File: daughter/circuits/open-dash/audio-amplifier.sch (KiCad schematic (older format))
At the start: 28 parts, among them J12 AudioJack_3.5TRS, J13 AudioJack_3.5TRS, J14 Conn_02x03_Odd_Even, T1 Audio_Transformer, T2 Audio_Transformer, T3 Audio_Transformer, T4 Audio_Transformer, U7 TDA7851F

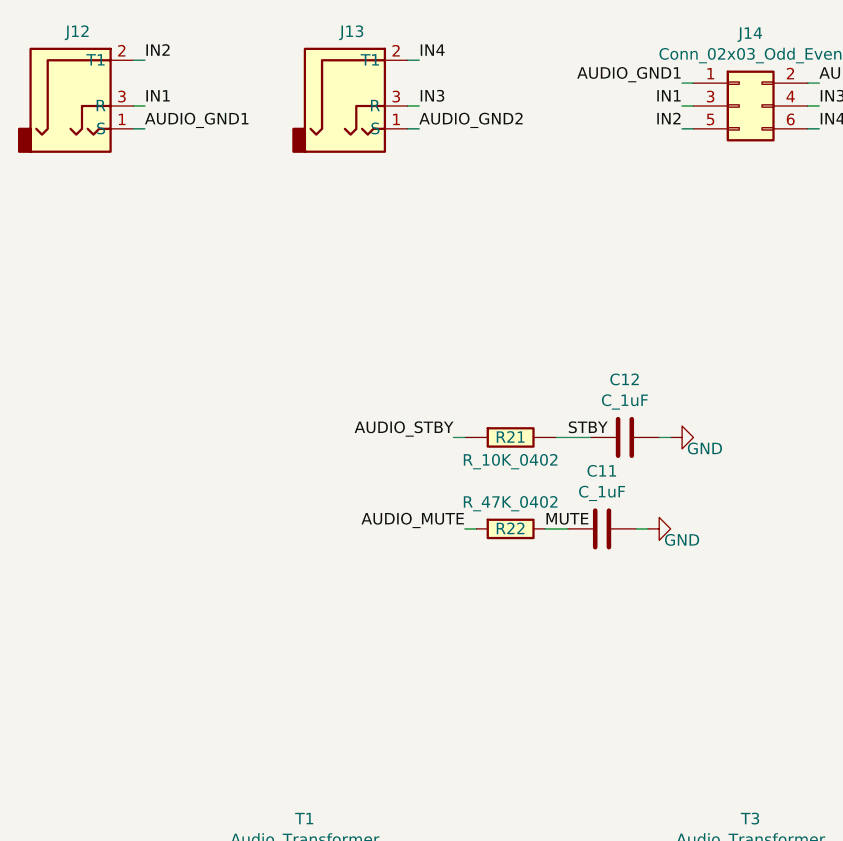
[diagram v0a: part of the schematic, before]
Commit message: send v1.4 to board house. Corrected source-drain on fets.
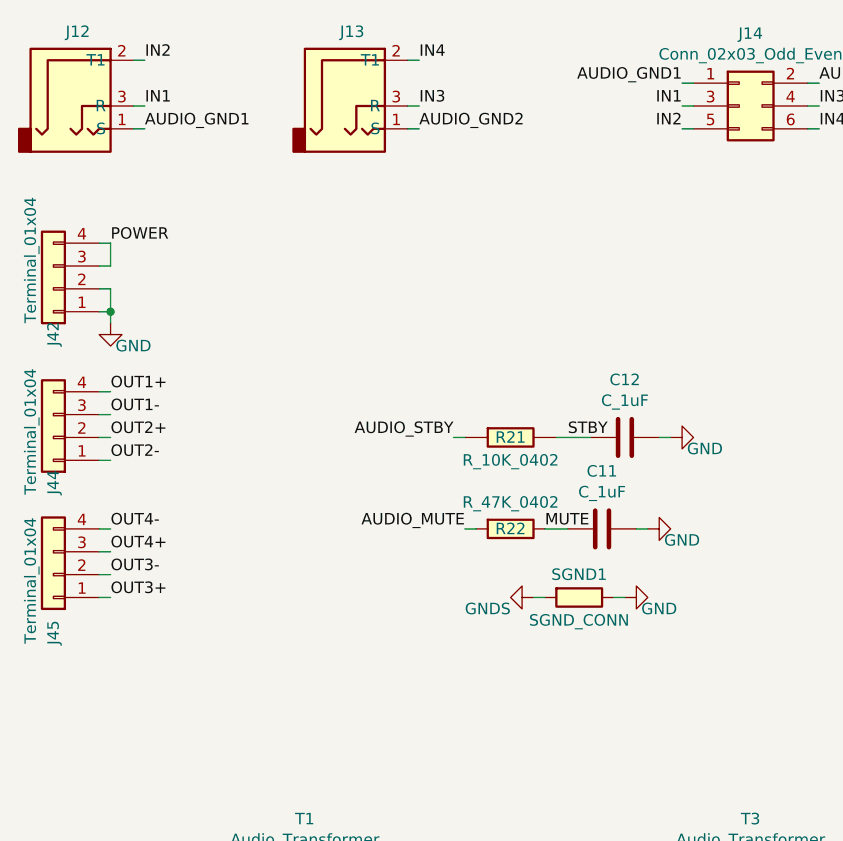
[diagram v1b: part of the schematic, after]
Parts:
- added J42, J44, J45: Terminal_01x04, Open_Automation:Terminal_1,5_4-G-5.08_1x04_P5.08mm_Horizontal, symbol Open_Automation:Terminal_01x04
- added SGND1: SGND_CONN, Open_Automation:SGND_CONN, symbol Open_Automation:SGND_CONN
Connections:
- net AUDIO_POWER: now also J42.3 (Pin_3), J42.4 (Pin_4)
- net GND: now also J42.1 (Pin_1), J42.2 (Pin_2), SGND1.1
- net GNDS: now also SGND1.2
- net LF_AUDIO_OUT+: now also J44.4 (Pin_4)
- net LF_AUDIO_OUT-: now also J44.3 (Pin_3)
- net LR_AUDIO_OUT+: now also J45.1 (Pin_1)
- net LR_AUDIO_OUT-: now also J45.2 (Pin_2)
- net RF_AUDIO_OUT+: now also J44.2 (Pin_2)
- net RF_AUDIO_OUT-: now also J44.1 (Pin_1)
- net RR_AUDIO_OUT+: now also J45.3 (Pin_3)
- net RR_AUDIO_OUT-: now also J45.4 (Pin_4)

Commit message: updated schematic
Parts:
- removed C17: C_10uF, Capacitor_SMD:C_0805_2012Metric_Pad1.18x1.45mm_HandSolder, symbol Open_Automation:C_10uF
- added C17: C_1uF, Capacitor_SMD:C_0402_1005Metric_Pad0.74x0.62mm_HandSolder, symbol Open_Automation:C_1uF
- added C28: C_47uF, Capacitor_SMD:C_1210_3225Metric_Pad1.33x2.70mm_HandSolder, symbol Open_Automation:C_47uF
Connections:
- net GND: now also C17.2, C28.2
- net SVR: now also C17.1, C28.1
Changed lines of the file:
@@
-$EndComp
-$Comp
-L Open_Automation:C_10uF C17
-U 1 1 6051CBF8
-P 7300 5500
-F 0 "C17" H 7200 5600 50  0000 L CNN
-F 1 "C_10uF" H 7000 5400 50  0000 L CNN
-F 2 "Capacitor_SMD:C_0805_2012Metric_Pad1.18x1.45mm_HandSolder" H 7550 5950 50  0001 C CNN
-F 3 "https://datasheet.lcsc.com/szlcsc/Samsung-Electro-Mechanics-CL21A106KAYNNNE_C15850.pdf" H 7300 5250 50  0001 C CNN
-F 4 "CL21A106KAYNNNE" H 7350 6050 60  0001 C CNN "Part Number"
-F 5 "C15850" H 7300 6150 50  0001 C CNN "LCSC"
-	1    7300 5500
-	1    0    0    -1
 $EndComp
 $Comp
@@
 	1200 3300 1200 3400
 Connection ~ 1200 3400
+$Comp
+L Open_Automation:C_47uF C28
+U 1 1 6200CB35
+P 7300 5500
+F 0 "C28" H 7100 5500 50  0000 L CNN
+F 1 "C_47uF" H 7000 5400 50  0000 L CNN
+F 2 "Capacitor_SMD:C_1210_3225Metric_Pad1.33x2.70mm_HandSolder" H 7400 5800 50  0001 C CNN
+F 3 "https://datasheet.lcsc.com/szlcsc/2007130932_Taiyo-Yuden-TMK325ABJ476MM-P_C90142.pdf" H 7300 5250 50  0001 C CNN
+F 4 "C90142" H 7300 5900 50  0001 C CNN "LCSC"
+F 5 "TMK325ABJ476MM-P" H 7425 5700 60  0001 C CNN "Part Number"
+	1    7300 5500
+	1    0    0    -1
+$EndComp
+$Comp
+L Open_Automation:C_1uF C17
+U 1 1 6200ED21
+P 6850 5500
+F 0 "C17" H 6650 5500 50  0000 L CNN
+F 1 "C_1uF" H 6600 5400 50  0000 L CNN
+F 2 "Capacitor_SMD:C_0402_1005Metric_Pad0.74x0.62mm_HandSolder" H 6950 5800 50  0001 C CNN
+F 3 "https://datasheet.lcsc.com/szlcsc/Samsung-Electro-Mechanics-CL05A105KA5NQNC_C52923.pdf" H 6850 5250 50  0001 C CNN
+F 4 "C52923" H 6850 5900 50  0001 C CNN "LCSC"
+F 5 "CL05A105KA5NQNC" H 6975 5700 60  0001 C CNN "Part Number"
+	1    6850 5500
+	1    0    0    -1
+$EndComp
+Wire Wire Line
+	6850 5650 6850 5700
+Wire Wire Line
+	6850 5700 7300 5700
+Connection ~ 7300 5700
+Wire Wire Line
+	6850 5350 7300 5350
+Connection ~ 7300 5350
 $EndSCHEMATC
